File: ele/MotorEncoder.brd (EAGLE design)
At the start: 24 x 16 mm, 18 parts, among them X1 PHB_1MM27_2X03_SNT_S, X2 PHB_1MM27_2X03_SNT_S

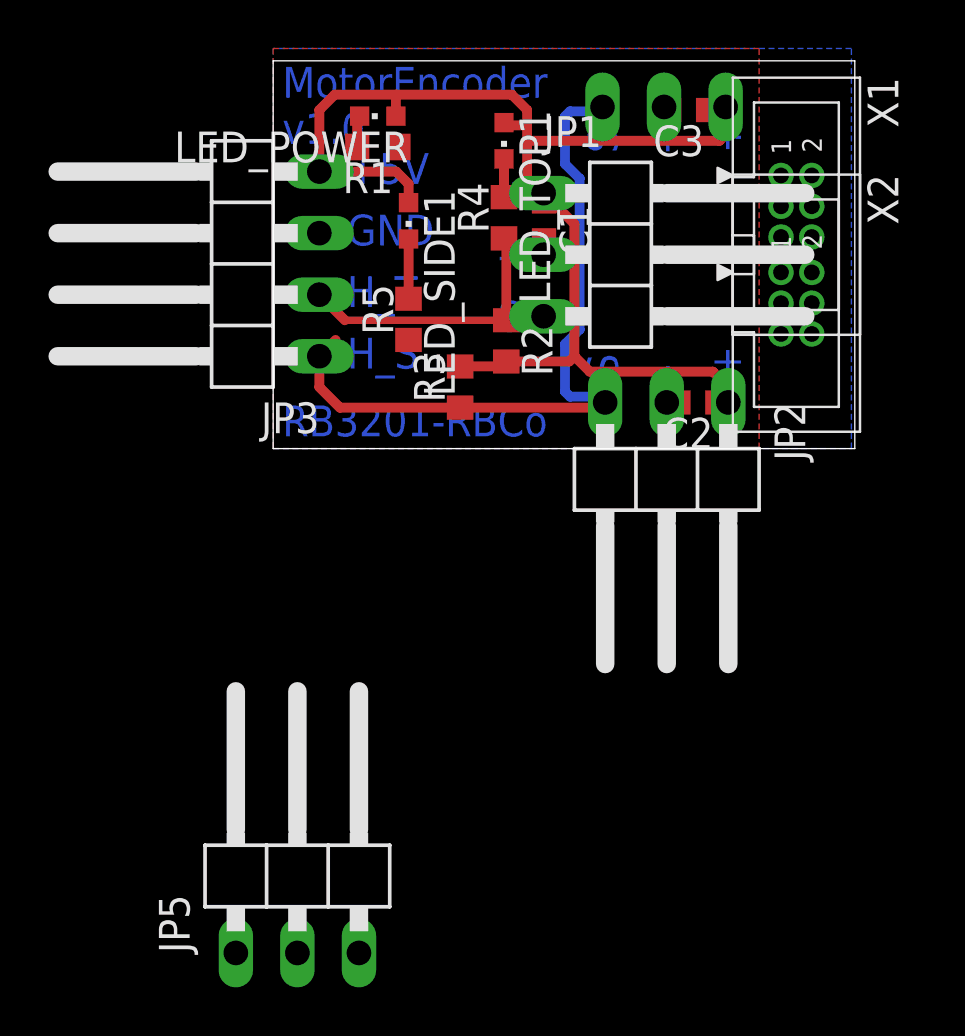
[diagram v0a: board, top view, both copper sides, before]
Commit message: ele: MotorEncoder - finish layout of PCB
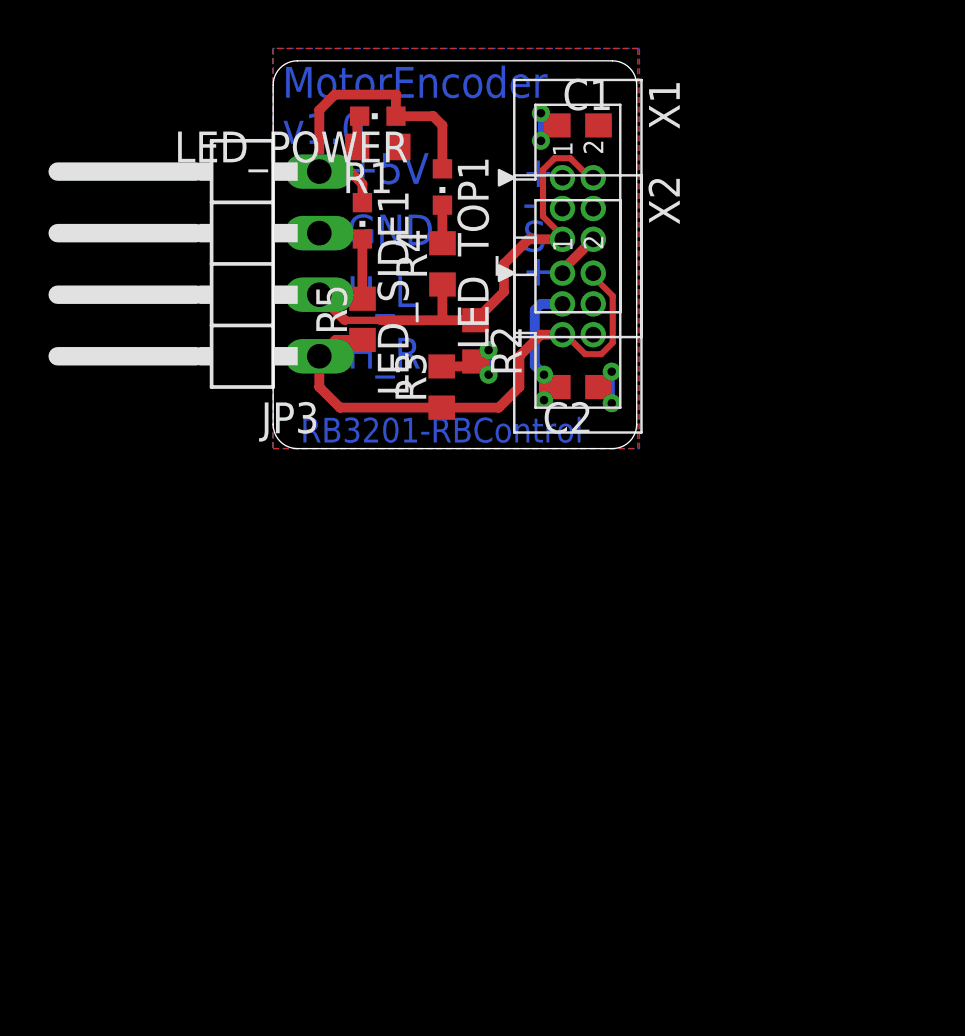
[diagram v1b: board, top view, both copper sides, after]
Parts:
- removed C3: 100n/6,3V,, rcl:C0603
- removed JP1: HAL_TOP, pinhead:1X03/90
- removed JP2: HAL_SIDE_R, pinhead:1X03/90
- removed JP4, JP5: HAL_SIDE_L, pinhead:1X03/90
- moved X1 9.02 mm to (12.6, 9.91)
- moved X2 9.02 mm to (12.6, 5.97)
- moved C2 4.99 mm to (12.6, 2.54)
- moved C1 4.18 mm to (12.6, 13.3), turned to 0 degrees
- moved R4 3.17 mm to (6.99, 7.62)
- moved LED_TOP1 3.17 mm to (6.99, 10.8)
- moved LED_SIDE1 1.91 mm to (3.68, 9.40)
- moved R5 1.91 mm to (3.68, 5.33)
- moved R2 1.27 mm to (8.35, 4.45)
- moved R3 0.76 mm to (6.95, 2.54)
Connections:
- removed net HAL_SIDE: JP2.3, JP3.1, JP4.3, R3.1, R5.1, X2.5, X2.6
- removed net HAL_TOP: JP1.3, JP3.2, R2.1, R4.1, X1.5, X1.6
- new net HAL_LEFT: JP3.2, R2.1, R4.1, X1.2, X1.5
- new net HAL_RIGHT: JP3.1, R3.1, R5.1, X2.2, X2.5
- net +5V: now also X1.6, X2.6; no longer C3.1, JP1.1, JP2.1, JP4.1, X1.2, X2.2
- net GND: no longer C3.2, JP1.2, JP2.2, JP4.2
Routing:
- net HAL_SIDE: track 29.9 -> 0.00 mm
- net +5V: track 52.7 -> 25.5 mm, vias 0 -> 6
- net HAL_LEFT: track 0.00 -> 23.7 mm
- net HAL_RIGHT: track 0.00 -> 21.6 mm
- net HAL_TOP: track 13.5 -> 0.00 mm
- net GND: track 1.21 -> 6.17 mm, vias 0 -> 2
- added copper zone on layer 16, net +5V
- removed copper zone on layer 16, net GND
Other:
- board size 24 x 16 mm -> 15 x 16 mm
- board text added: "10k"
- board text added: "H_L"
- board text added: "H_R"
- board text added: "L:"
- board text added: "R:"
- board text added: "RB3201-RBControl"
- board text removed: "H_S"
- board text removed: "H_T"
- board text removed: "RB3201-RBCo"
